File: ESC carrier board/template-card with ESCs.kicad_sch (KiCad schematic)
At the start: 18 parts, among them J3 Conn_01x04_Pin, J4 Conn_01x04_Pin, J5 Conn_01x04_Pin, U2 ESC, U4 ESC, U6 ESC

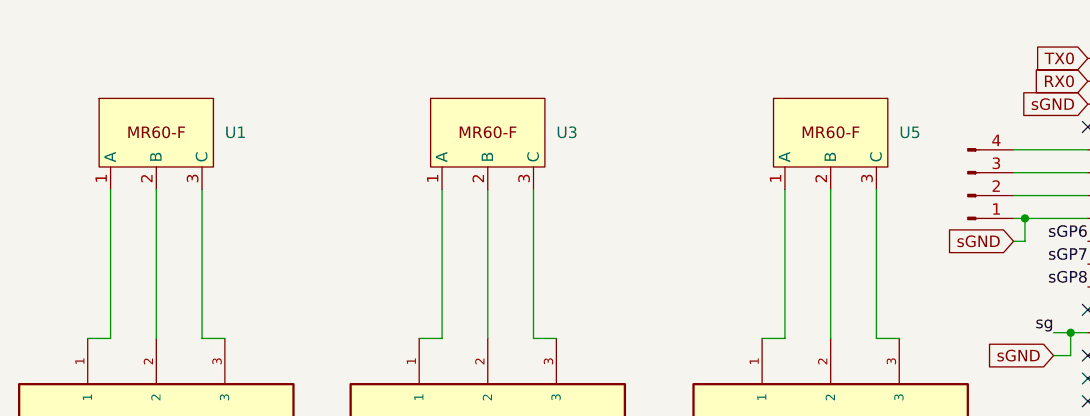
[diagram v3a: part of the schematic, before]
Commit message: changed to mr60PW-M connector
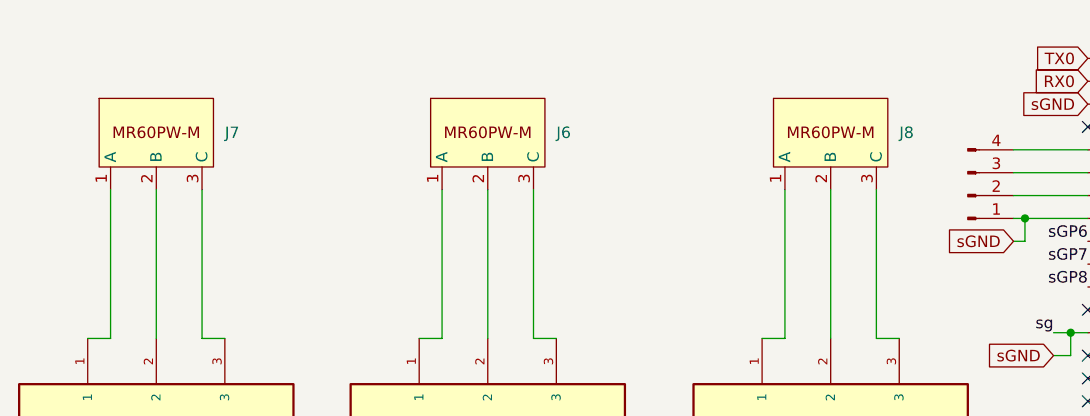
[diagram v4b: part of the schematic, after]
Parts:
- removed U1, U3, U5: ~, 2024-backplane:MR60-F, symbol 2024-backplane:MR60-F
- added J6, J7, J8: ~, 2024-backplane:MR60PW-M, symbol 2024-backplane:MR60PW-M
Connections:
- net at U4.1: now also J6.1 (A)
- net at U4.2: now also J6.2 (B)
- net at U4.3: now also J6.3 (C)
- net at U2.1: now also J7.1 (A)
- net at U2.2: now also J7.2 (B)
- net at U2.3: now also J7.3 (C)
- net at U6.1: now also J8.1 (A)
- net at U6.2: now also J8.2 (B)
- net at U6.3: now also J8.3 (C)
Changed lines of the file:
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@@
+    )
+  )
+  (symbol (lib_id "2024-backplane:MR60PW-M") (at 41.91 31.75 0) (unit 1)
+    (in_bom yes) (on_board yes) (dnp no) (fields_autoplaced)
+    (property "Reference" "J7" (at 45.72 25.4 0)
+      (effects (font (size 1.27 1.27)) (justify left))
+    )
+    (property "Value" "~" (at 38.1 25.4 0)
+      (effects (font (size 1.27 1.27)))
+    )
+    (property "Footprint" "2024-backplane:MR60PW-M" (at 35.56 11.43 0)
+      (effects (font (size 1.27 1.27)) hide)
+    )
+    (property "Datasheet" "https://www.tme.com/Document/fd4b3517709a946d7b01cf4810656931/MR60PW-M.pdf" (at 36.83 13.97 0)
+      (effects (font (size 1.27 1.27)) hide)
+    )
+    (pin "3")
+    (pin "1")
+    (pin "2")
+    (instances
+      (project "template-card with ESCs"
+        (path "/447f7668-e44a-4076-b3cb-4e0f6120b53c"
+          (reference "J7") (unit 1)
+        )
+      )
     )
   )
@@
     )
   )
-  (symbol (lib_id "2024-backplane:MR60-F") (at 78.74 31.75 0) (unit 1)
-    (in_bom yes) (on_board yes) (dnp no) (fields_autoplaced)
-    (property "Reference" "U3" (at 82.55 25.4 0)
-      (effects (font (size 1.27 1.27)) (justify left))
-    )
-    (property "Value" "~" (at 74.93 25.4 0)
-      (effects (font (size 1.27 1.27)))
-    )
-    (property "Footprint" "2024-backplane:MR60-F" (at 74.93 25.4 0)
-      (effects (font (size 1.27 1.27)) hide)
-    )
-    (property "Datasheet" "" (at 74.93 25.4 0)
-      (effects (font (size 1.27 1.27)) hide)
-    )
-    (pin "2")
-    (pin "3")
-    (pin "1")
-    (instances
-      (project "template-card with ESCs"
-        (path "/447f7668-e44a-4076-b3cb-4e0f6120b53c"
-          (reference "U3") (unit 1)
-        )
-      )
-    )
-  )
   (symbol (lib_id "power:GND2") (at 106.68 132.715 0) (unit 1)
     (in_bom yes) (on_board yes) (dnp no)
@@
     )
   )
-  (symbol (lib_id "2024-backplane:MR60-F") (at 116.84 31.75 0) (unit 1)
-    (in_bom yes) (on_board yes) (dnp no) (fields_autoplaced)
-    (property "Reference" "U5" (at 120.65 25.4 0)
-      (effects (font (size 1.27 1.27)) (justify left))
-    )
-    (property "Value" "~" (at 113.03 25.4 0)
-      (effects (font (size 1.27 1.27)))
-    )
-    (property "Footprint" "2024-backplane:MR60-F" (at 113.03 25.4 0)
-      (effects (font (size 1.27 1.27)) hide)
-    )
-    (property "Datasheet" "" (at 113.03 25.4 0)
-      (effects (font (size 1.27 1.27)) hide)
-    )
-    (pin "2")
-    (pin "3")
-    (pin "1")
-    (instances
-      (project "template-card with ESCs"
-        (path "/447f7668-e44a-4076-b3cb-4e0f6120b53c"
-          (reference "U5") (unit 1)
-        )
-      )
-    )
-  )
   (symbol (lib_id "Jumper:SolderJumper_3_Open") (at 199.39 27.94 90) (unit 1)
     (in_bom yes) (on_board yes) (dnp no) (fields_autoplaced)
@@
     )
   )
-  (symbol (lib_id "2024-backplane:MR60-F") (at 41.91 31.75 0) (unit 1)
-    (in_bom yes) (on_board yes) (dnp no) (fields_autoplaced)
-    (property "Reference" "U1" (at 45.72 25.4 0)
-      (effects (font (size 1.27 1.27)) (justify left))
-    )
-    (property "Value" "~" (at 38.1 25.4 0)
-      (effects (font (size 1.27 1.27)))
-    )
-    (property "Footprint" "2024-backplane:MR60-F" (at 38.1 25.4 0)
-      (effects (font (size 1.27 1.27)) hide)
-    )
-    (property "Datasheet" "" (at 38.1 25.4 0)
-      (effects (font (size 1.27 1.27)) hide)
-    )
-    (pin "2")
-    (pin "3")
-    (pin "1")
-    (instances
-      (project "template-card with ESCs"
-        (path "/447f7668-e44a-4076-b3cb-4e0f6120b53c"
-          (reference "U1") (unit 1)
-        )
-      )
+  (symbol (lib_id "2024-backplane:MR60PW-M") (at 78.74 31.75 0) (unit 1)
+    (in_bom yes) (on_board yes) (dnp no) (fields_autoplaced)
+    (property "Reference" "J6" (at 82.55 25.4 0)
+      (effects (font (size 1.27 1.27)) (justify left))
+    )
+    (property "Value" "~" (at 74.93 25.4 0)
+      (effects (font (size 1.27 1.27)))
+    )
+    (property "Footprint" "2024-backplane:MR60PW-M" (at 72.39 11.43 0)
+      (effects (font (size 1.27 1.27)) hide)
+    )
+    (property "Datasheet" "https://www.tme.com/Document/fd4b3517709a946d7b01cf4810656931/MR60PW-M.pdf" (at 73.66 13.97 0)
+      (effects (font (size 1.27 1.27)) hide)
+    )
+    (pin "3")
+    (pin "1")
+    (pin "2")
+    (instances
+      (project "template-card with ESCs"
+        (path "/447f7668-e44a-4076-b3cb-4e0f6120b53c"
+          (reference "J6") (unit 1)
+        )
+      )
+    )
+  )
+  (symbol (lib_id "2024-backplane:MR60PW-M") (at 116.84 31.75 0) (unit 1)
+    (in_bom yes) (on_board yes) (dnp no) (fields_autoplaced)
+    (property "Reference" "J8" (at 120.65 25.4 0)
+      (effects (font (size 1.27 1.27)) (justify left))
+    )
+    (property "Value" "~" (at 113.03 25.4 0)
+      (effects (font (size 1.27 1.27)))
+    )
+    (property "Footprint" "2024-backplane:MR60PW-M" (at 110.49 11.43 0)
+      (effects (font (size 1.27 1.27)) hide)
+    )
+    (property "Datasheet" "https://www.tme.com/Document/fd4b3517709a946d7b01cf4810656931/MR60PW-M.pdf" (at 111.76 13.97 0)
+      (effects (font (size 1.27 1.27)) hide)
+    )
+    (pin "3")
+    (pin "1")
+    (pin "2")
+    (instances
+      (project "template-card with ESCs"
+        (path "/447f7668-e44a-4076-b3cb-4e0f6120b53c"
+          (reference "J8") (unit 1)
+        )
+      )

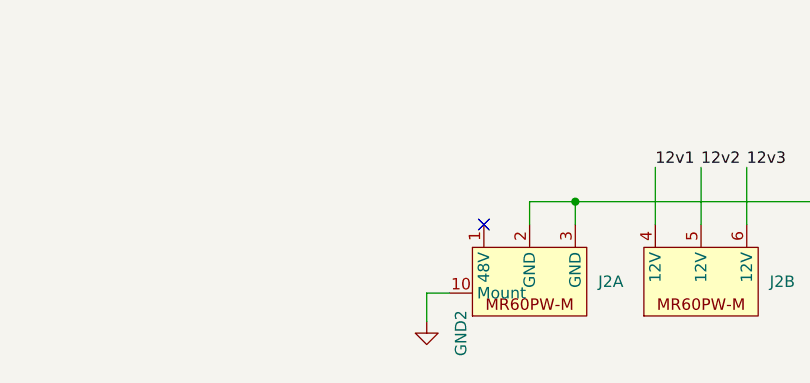
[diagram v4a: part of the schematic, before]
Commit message: Modified Board for easier ESC mounting
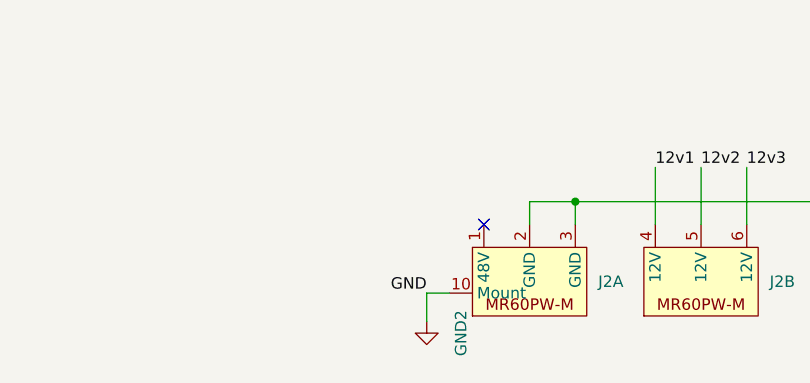
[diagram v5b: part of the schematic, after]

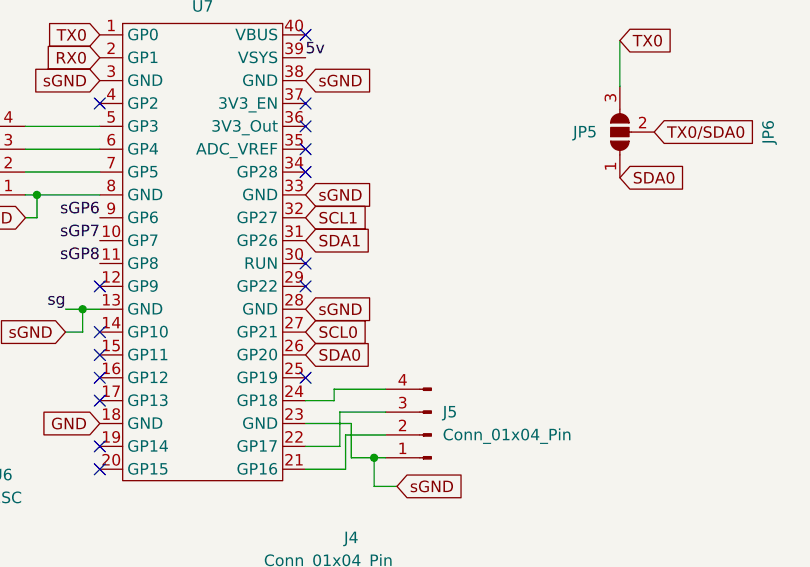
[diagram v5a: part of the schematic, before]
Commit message: Shorted I2C
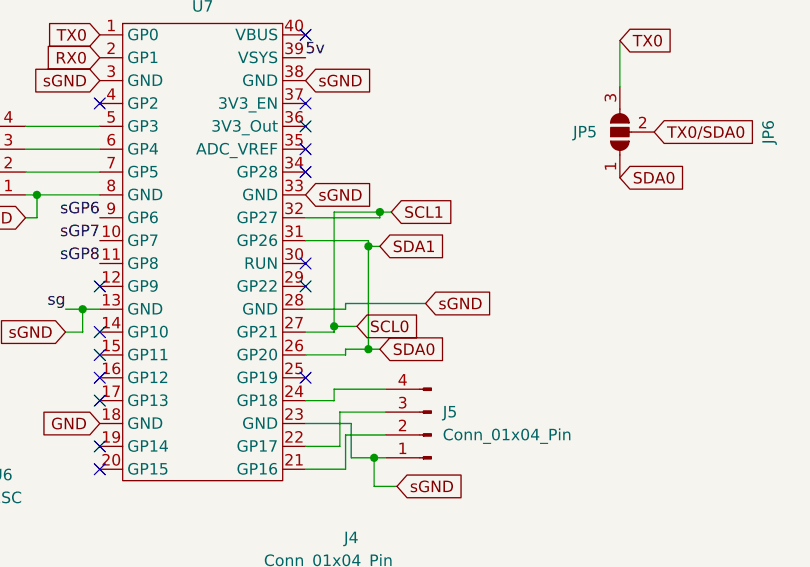
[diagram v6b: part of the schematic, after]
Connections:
- net SCL1 is gone; now on net SCL0: JP2.2 (B), U7.32 (GP27)
- net SDA1 is gone; now on net SDA0: JP1.2 (B), U7.31 (GP26)
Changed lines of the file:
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@@
+	)
+	(junction
+		(at 167.64 49.53)
+		(diameter 0)
+		(color 0 0 0 0)
 	)
 	(junction
@@
 	)
 	(junction
+		(at 171.45 52.07)
+		(diameter 0)
+		(color 0 0 0 0)
+	)
+	(junction
 		(at 156.21 119.38)
 		(diameter 0)
@@
 	)
 	(junction
+		(at 172.72 36.83)
+		(diameter 0)
+		(color 0 0 0 0)
+	)
+	(junction
 		(at 229.235 89.535)
 		(diameter 0)
 		(color 0 0 0 0)
 	)
+	(junction
+		(at 171.45 40.64)
+		(diameter 0)
+		(color 0 0 0 0)
+	)
 	(no_connect
 		(at 164.465 29.845)
@@
 	(wire
 		(pts
+			(xy 172.72 40.64) (xy 171.45 40.64)
+		)
+		(stroke
+			(width 0)
+			(type default)
+		)
+	)
+	(wire
+		(pts
 			(xy 43.18 31.75) (xy 43.18 48.26)
 		)
@@
 	(wire
 		(pts
+			(xy 168.91 52.705) (xy 164.465 52.705)
+		)
+		(stroke
+			(width 0)
+			(type default)
+		)
+	)
+	(wire
+		(pts
+			(xy 172.72 37.465) (xy 164.465 37.465)
+		)
+		(stroke
+			(width 0)
+			(type default)
+		)
+	)
+	(wire
+		(pts
 			(xy 118.11 119.38) (xy 123.19 119.38)
 		)
@@
 	(wire
 		(pts
+			(xy 171.45 40.005) (xy 164.465 40.005)
+		)
+		(stroke
+			(width 0)
+			(type default)
+		)
+	)
+	(wire
+		(pts
 			(xy 168.275 62.865) (xy 168.275 59.055)
 		)
@@
 	(wire
 		(pts
+			(xy 172.72 36.83) (xy 167.64 36.83)
+		)
+		(stroke
+			(width 0)
+			(type default)
+		)
+	)
+	(wire
+		(pts
 			(xy 168.275 59.055) (xy 173.355 59.055)
 		)
@@
 	(wire
 		(pts
+			(xy 173.99 36.83) (xy 172.72 36.83)
+		)
+		(stroke
+			(width 0)
+			(type default)
+		)
+	)
+	(wire
+		(pts
+			(xy 168.91 52.07) (xy 168.91 52.705)
+		)
+		(stroke
+			(width 0)
+			(type default)
+		)
+	)
+	(wire
+		(pts
 			(xy 33.02 48.26) (xy 30.48 48.26)
 		)
@@
 	(wire
 		(pts
+			(xy 168.91 46.99) (xy 168.91 47.625)
+		)
+		(stroke
+			(width 0)
+			(type default)
+		)
+	)
+	(wire
+		(pts
 			(xy 224.79 81.28) (xy 224.79 92.71)
 		)
@@
 	(wire
 		(pts
+			(xy 168.91 47.625) (xy 164.465 47.625)
+		)
+		(stroke
+			(width 0)
+			(type default)
+		)
+	)
+	(wire
+		(pts
 			(xy 134.62 37.465) (xy 133.35 37.465)
 		)
@@
 	(wire
 		(pts
+			(xy 172.72 36.83) (xy 172.72 37.465)
+		)
+		(stroke
+			(width 0)
+			(type default)
+		)
+	)
+	(wire
+		(pts
 			(xy 137.16 115.57) (xy 137.16 121.92)
 		)
@@
 	(wire
 		(pts
+			(xy 167.64 36.83) (xy 167.64 49.53)
+		)
+		(stroke
+			(width 0)
+			(type default)
+		)
+	)
+	(wire
+		(pts
 			(xy 224.155 92.71) (xy 224.79 92.71)
 		)
@@
 	(wire
 		(pts
+			(xy 171.45 52.07) (xy 168.91 52.07)
+		)
+		(stroke
+			(width 0)
+			(type default)
+		)
+	)
+	(wire
+		(pts
 			(xy 169.545 64.135) (xy 172.085 64.135)
 		)
@@
 	(wire
 		(pts
+			(xy 172.72 52.07) (xy 171.45 52.07)
+		)
+		(stroke
+			(width 0)
+			(type default)
+		)
+	)
+	(wire
+		(pts
+			(xy 167.64 49.53) (xy 167.64 50.165)
+		)
+		(stroke
+			(width 0)
+			(type default)
+		)
+	)
+	(wire
+		(pts
 			(xy 244.475 89.535) (xy 247.65 89.535)
 		)
@@
 	(wire
 		(pts
+			(xy 167.64 50.165) (xy 164.465 50.165)
+		)
+		(stroke
+			(width 0)
+			(type default)
+		)
+	)
+	(wire
+		(pts
 			(xy 113.03 31.75) (xy 113.03 48.26)
 		)
@@
 	(wire
 		(pts
+			(xy 171.45 40.64) (xy 171.45 40.005)
+		)
+		(stroke
+			(width 0)
+			(type default)
+		)
+	)
+	(wire
+		(pts
 			(xy 38.1 31.75) (xy 38.1 48.26)
 		)
@@
 	(wire
 		(pts
+			(xy 170.18 49.53) (xy 167.64 49.53)
+		)
+		(stroke
+			(width 0)
+			(type default)
+		)
+	)
+	(wire
+		(pts
 			(xy 137.795 47.625) (xy 139.7 47.625)
 		)
@@
 	(wire
 		(pts
+			(xy 177.8 46.99) (xy 168.91 46.99)
+		)
+		(stroke
+			(width 0)
+			(type default)
+		)
+	)
+	(wire
+		(pts
 			(xy 74.93 48.26) (xy 74.93 31.75)
+		)
+		(stroke
+			(width 0)
+			(type default)
+		)
+	)
+	(wire
+		(pts
+			(xy 171.45 40.64) (xy 171.45 52.07)
 		)
 		(stroke
@@
 	(global_label "SCL1"
 		(shape input)
-		(at 164.465 37.465 0)
-		(fields_autoplaced yes)
-		(effects
-			(font
-				(size 1.27 1.27)
-			)
-			(justify left)
-		)
-		(property "Intersheetrefs" "${INTERSHEET_REFS}"
-			(at 172.1673 37.465 0)
+		(at 173.99 36.83 0)
+		(fields_autoplaced yes)
+		(effects
+			(font
+				(size 1.27 1.27)
+			)
+			(justify left)
+		)
+		(property "Intersheetrefs" "${INTERSHEET_REFS}"
+			(at 181.6923 36.83 0)
 			(effects
 				(font
@@
 	(global_label "sGND"
 		(shape input)
-		(at 164.465 47.625 0)
-		(fields_autoplaced yes)
-		(effects
-			(font
-				(size 1.27 1.27)
-			)
-			(justify left)
-		)
-		(property "Intersheetrefs" "${INTERSHEET_REFS}"
-			(at 172.3488 47.625 0)
+		(at 177.8 46.99 0)
+		(fields_autoplaced yes)
+		(effects
+			(font
+				(size 1.27 1.27)
+			)
+			(justify left)
+		)
+		(property "Intersheetrefs" "${INTERSHEET_REFS}"
+			(at 185.6838 46.99 0)
 			(effects
 				(font
@@
 	(global_label "SDA0"
 		(shape input)
-		(at 164.465 52.705 0)
-		(fields_autoplaced yes)
-		(effects
-			(font
-				(size 1.27 1.27)
-			)
-			(justify left)
-		)
-		(property "Intersheetrefs" "${INTERSHEET_REFS}"
-			(at 172.2278 52.705 0)
+		(at 172.72 52.07 0)
+		(fields_autoplaced yes)
+		(effects
+			(font
+				(size 1.27 1.27)
+			)
+			(justify left)
+		)
+		(property "Intersheetrefs" "${INTERSHEET_REFS}"
+			(at 180.4828 52.07 0)
 			(effects
 				(font
@@
 	(global_label "SDA1"
 		(shape input)
-		(at 164.465 40.005 0)
-		(fields_autoplaced yes)
-		(effects
-			(font
-				(size 1.27 1.27)
-			)
-			(justify left)
-		)
-		(property "Intersheetrefs" "${INTERSHEET_REFS}"
-			(at 172.2278 40.005 0)
+		(at 172.72 40.64 0)
+		(fields_autoplaced yes)
+		(effects
+			(font
+				(size 1.27 1.27)
+			)
+			(justify left)
+		)
+		(property "Intersheetrefs" "${INTERSHEET_REFS}"
+			(at 180.4828 40.64 0)
 			(effects
 				(font
@@
 	(global_label "SCL0"
 		(shape input)
-		(at 164.465 50.165 0)
-		(fields_autoplaced yes)
-		(effects
-			(font
-				(size 1.27 1.27)
-			)
-			(justify left)
-		)
-		(property "Intersheetrefs" "${INTERSHEET_REFS}"
-			(at 172.1673 50.165 0)
-			(effects
-				(font
+		(at 170.18 49.53 0)
+		(fields_autoplaced yes)
+		(effects
+			(font
+				(size 1.27 1.27)
+			)
+			(justify left)
+		)
+		(property "Intersheetrefs" "${INTERSHEET_REFS}"
+			(at 177.8823 49.53 0)
+			(effects
+				(font
